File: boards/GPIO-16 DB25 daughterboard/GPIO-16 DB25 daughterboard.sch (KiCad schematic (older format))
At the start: 2 parts, among them P101 HEADER_A, P102 HEADER_B

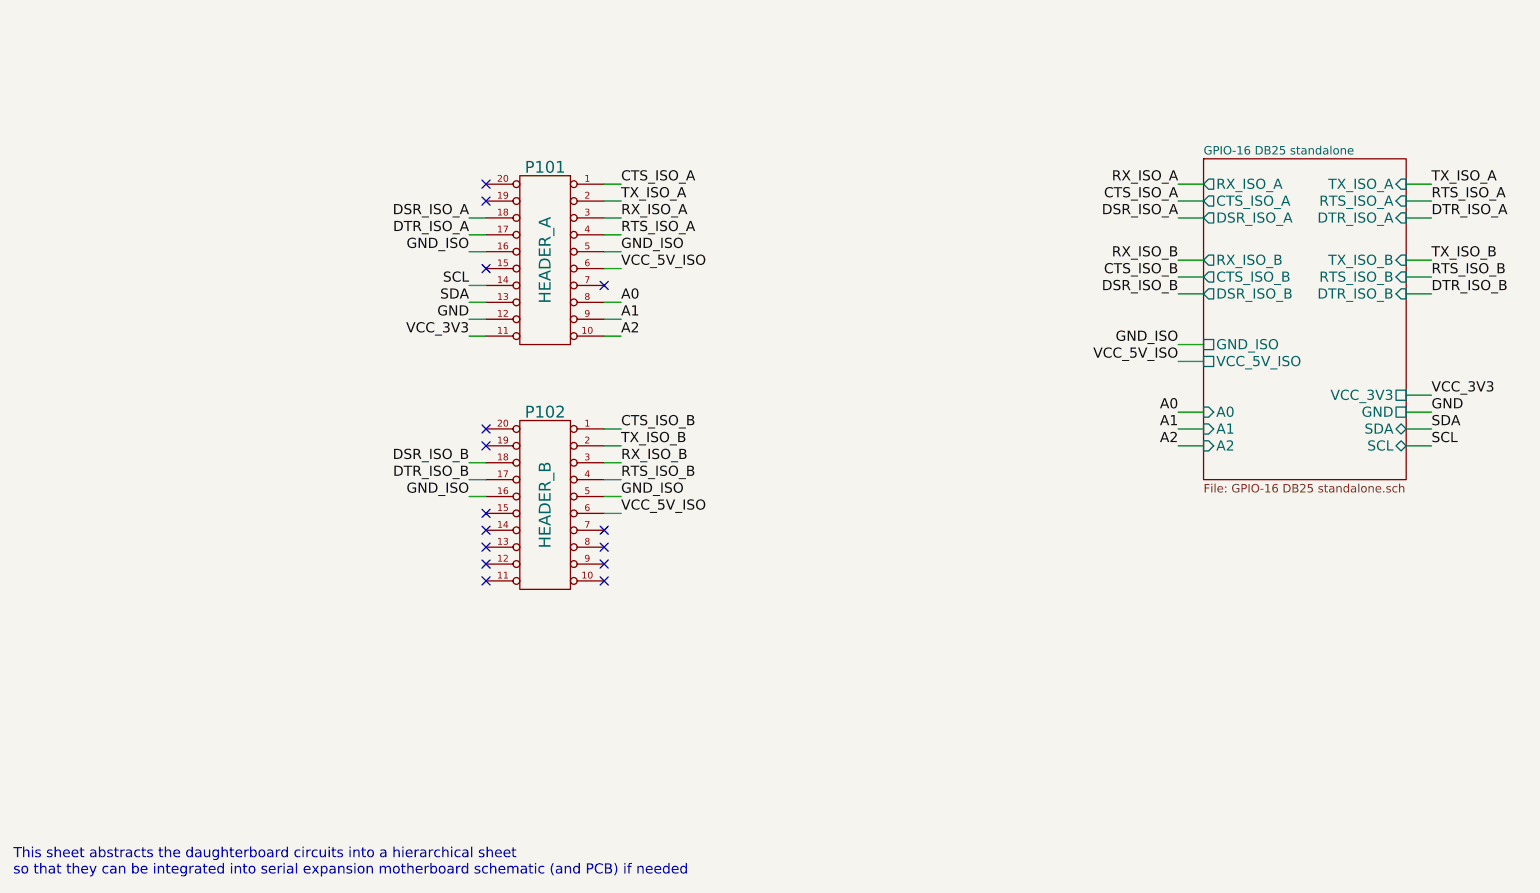
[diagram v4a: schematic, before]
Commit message: Updated GPIO-16 dboard to use new dboard_slot component
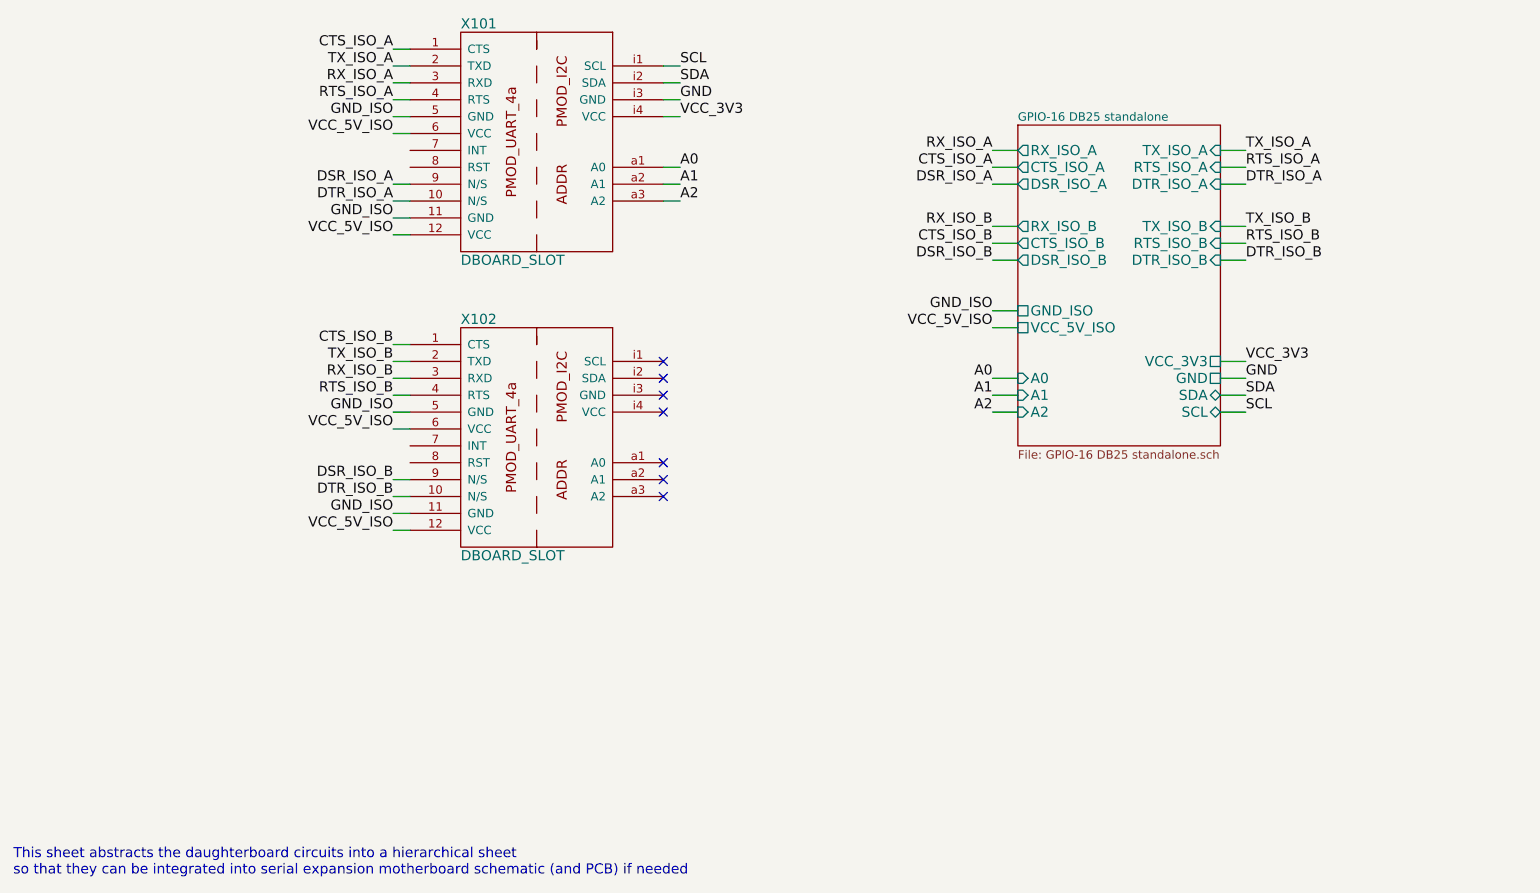
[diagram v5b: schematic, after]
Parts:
- removed P101: HEADER_A, symbol DIL20
- removed P102: HEADER_B, symbol DIL20
- added X101, X102: DBOARD_SLOT, ~, symbol DBOARD_SLOT
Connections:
- net A0: now also X101.a1 (A0)
- net A1: now also X101.a2 (A1)
- net A2: now also X101.a3 (A2)
- net CTS_ISO_A: now also X101.1 (CTS)
- net CTS_ISO_B: now also X102.1 (CTS)
- net DSR_ISO_A: now also X101.9 (N/S)
- net DSR_ISO_B: now also X102.9 (N/S)
- net DTR_ISO_A: now also X101.10 (N/S)
- net DTR_ISO_B: now also X102.10 (N/S)
- net GND: now also X101.i3 (GND)
- net GND_ISO: now also X101.11 (GND), X101.5 (GND), X102.11 (GND), X102.5 (GND)
- net RTS_ISO_A: now also X101.4 (RTS)
- net RTS_ISO_B: now also X102.4 (RTS)
- net RX_ISO_A: now also X101.3 (RXD)
- net RX_ISO_B: now also X102.3 (RXD)
- net SCL: now also X101.i1 (SCL)
- net SDA: now also X101.i2 (SDA)
- net TX_ISO_A: now also X101.2 (TXD)
- net TX_ISO_B: now also X102.2 (TXD)
- net VCC_3V3: now also X101.i4 (VCC)
- net VCC_5V_ISO: now also X101.12 (VCC), X101.6 (VCC), X102.12 (VCC), X102.6 (VCC)
- no-connect marks 15 -> 7
